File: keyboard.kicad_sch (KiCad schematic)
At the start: 14 parts, among them SW1 SW_SPDT, U1 STM32F072CBT6

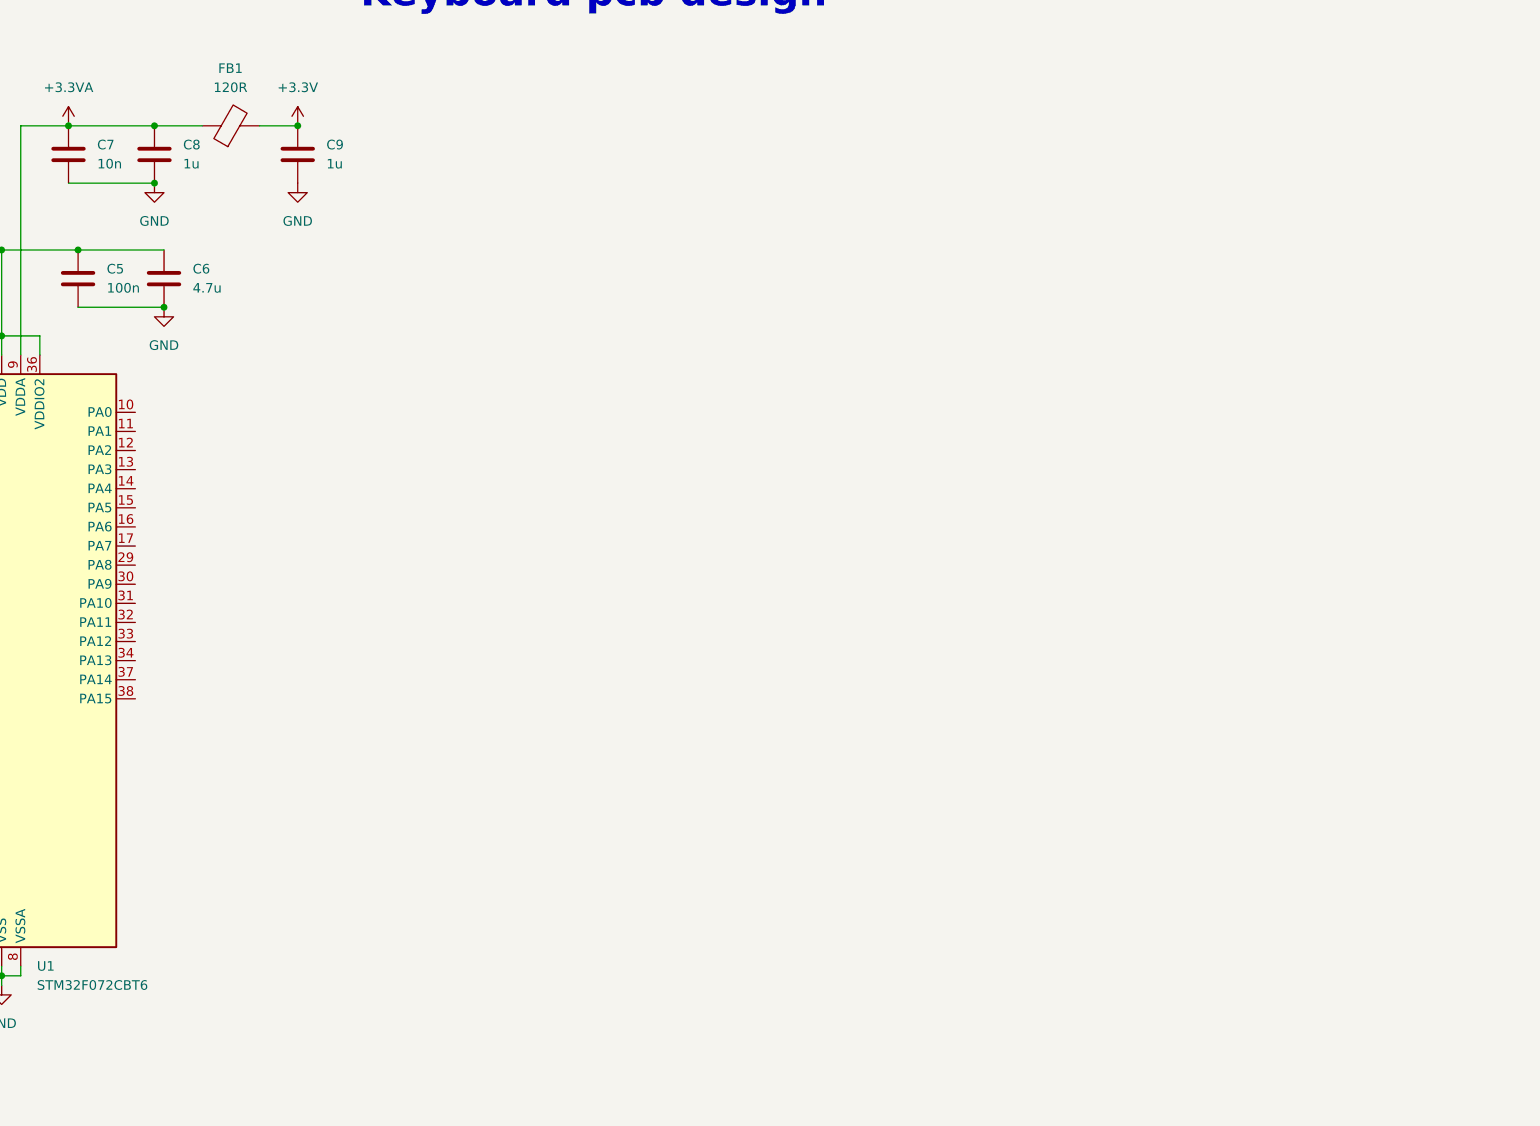
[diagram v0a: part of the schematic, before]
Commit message: Added keyboard matrix and leds
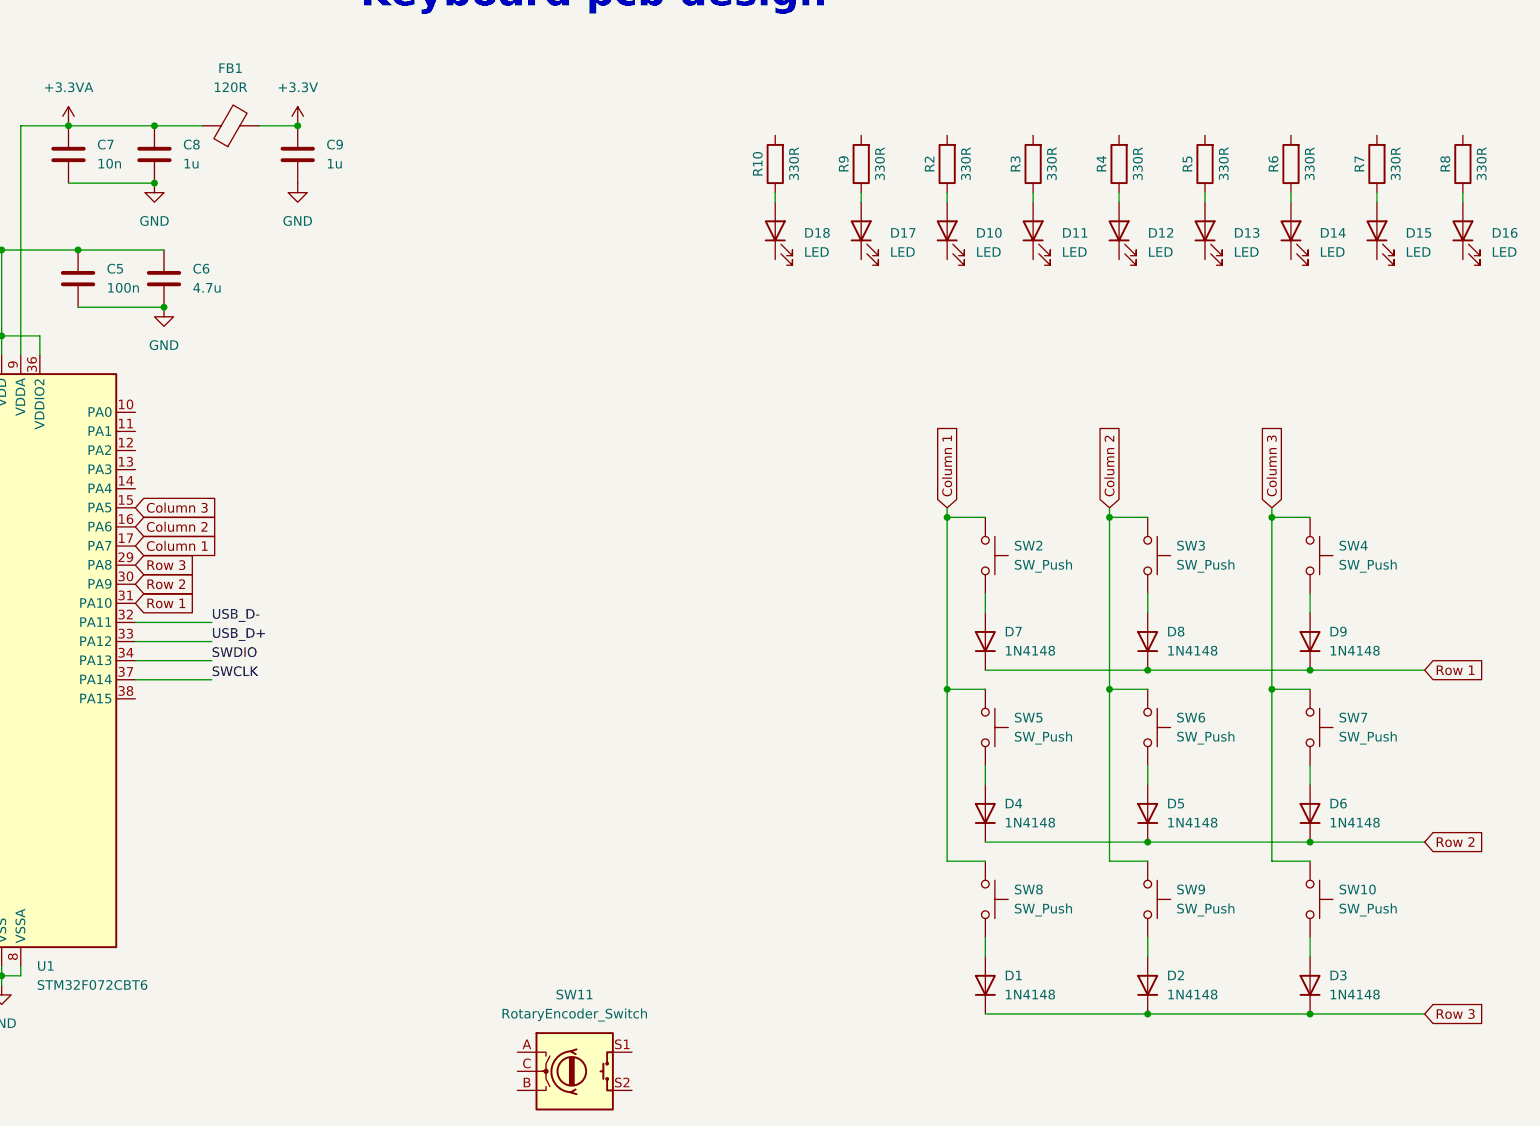
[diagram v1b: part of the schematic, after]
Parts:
- added D1, D2, D3, D4, D5, D6, D7, D8, D9: 1N4148, Diode_THT:D_DO-35_SOD27_P7.62mm_Horizontal, symbol Diode:1N4148
- added D10, D11, D12, D13, D14, D15, D16, D17, D18: LED, symbol Device:LED
- added R10, R2, R3, R4, R5, R6, R7, R8, R9: 330R, symbol Device:R
- added SW10, SW2, SW3, SW4, SW5, SW6, SW7, SW8, SW9: SW_Push, symbol Switch:SW_Push
- added SW11: RotaryEncoder_Switch, symbol Device:RotaryEncoder_Switch
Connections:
- net Column 3: now reaches U1.15 (PA5)
- net Column 3: now also SW10.1, SW4.1, SW7.1
- net Column 2: now reaches U1.16 (PA6)
- net Column 2: now also SW3.1, SW6.1, SW9.1
- net Column 1: now reaches U1.17 (PA7)
- net Column 1: now also SW2.1, SW5.1, SW8.1
- net Row 3: now reaches U1.29 (PA8)
- net Row 3: now also D1.1 (K), D2.1 (K), D3.1 (K)
- net Row 2: now reaches U1.30 (PA9)
- net Row 2: now also D4.1 (K), D5.1 (K), D6.1 (K)
- net Row 1: now reaches U1.31 (PA10)
- net Row 1: now also D7.1 (K), D8.1 (K), D9.1 (K)
- net USB_D-: now reaches U1.32 (PA11)
- net USB_D+: now reaches U1.33 (PA12)
- net SWDIO: now reaches U1.34 (PA13)
- net SWCLK: now reaches U1.37 (PA14)
- new net: D4.2 (A), SW5.2
- new net: D14.2 (A), R6.1
- new net: D18.2 (A), R10.1
- new net: D15.2 (A), R7.1
- new net: D17.2 (A), R9.1
- new net: D1.2 (A), SW8.2
- new net: D10.2 (A), R2.1
- new net: D13.2 (A), R5.1
- new net: D5.2 (A), SW6.2
- new net: D11.2 (A), R3.1
- new net: D6.2 (A), SW7.2
- new net: D2.2 (A), SW9.2
- new net: D16.2 (A), R8.1
- new net: D3.2 (A), SW10.2
- new net: D7.2 (A), SW2.2
- new net: D8.2 (A), SW3.2
- new net: D9.2 (A), SW4.2
- new net: D12.2 (A), R4.1

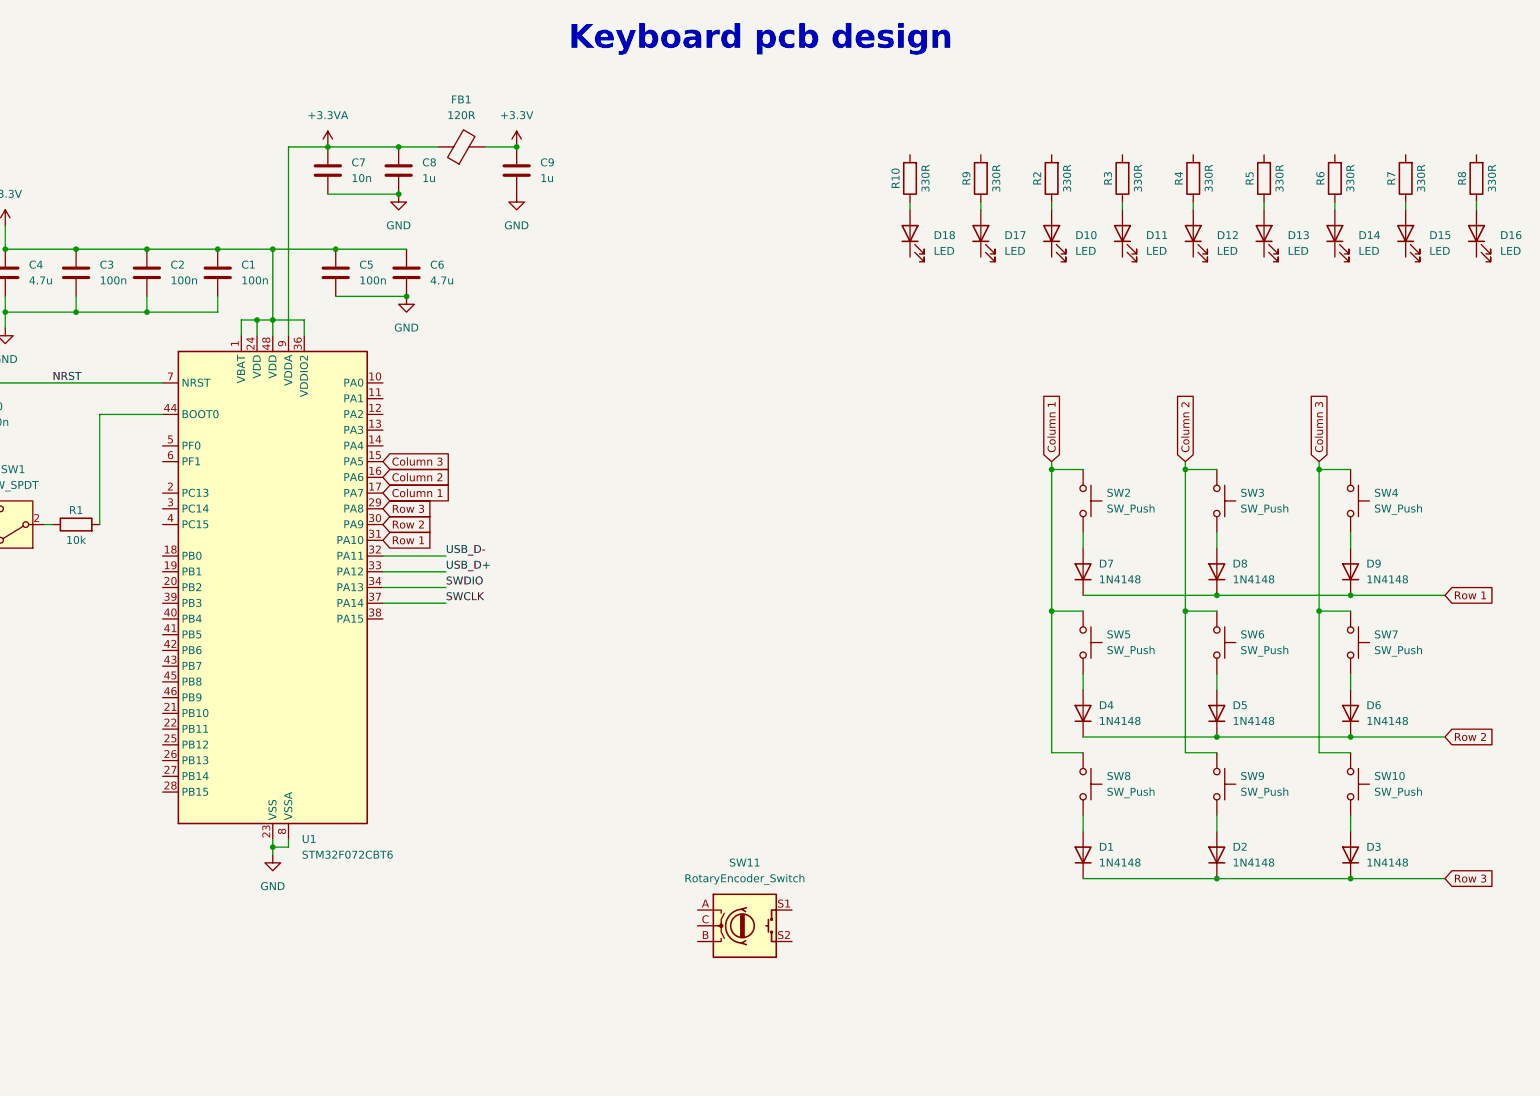
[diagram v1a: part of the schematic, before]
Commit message: Added rotary encoder
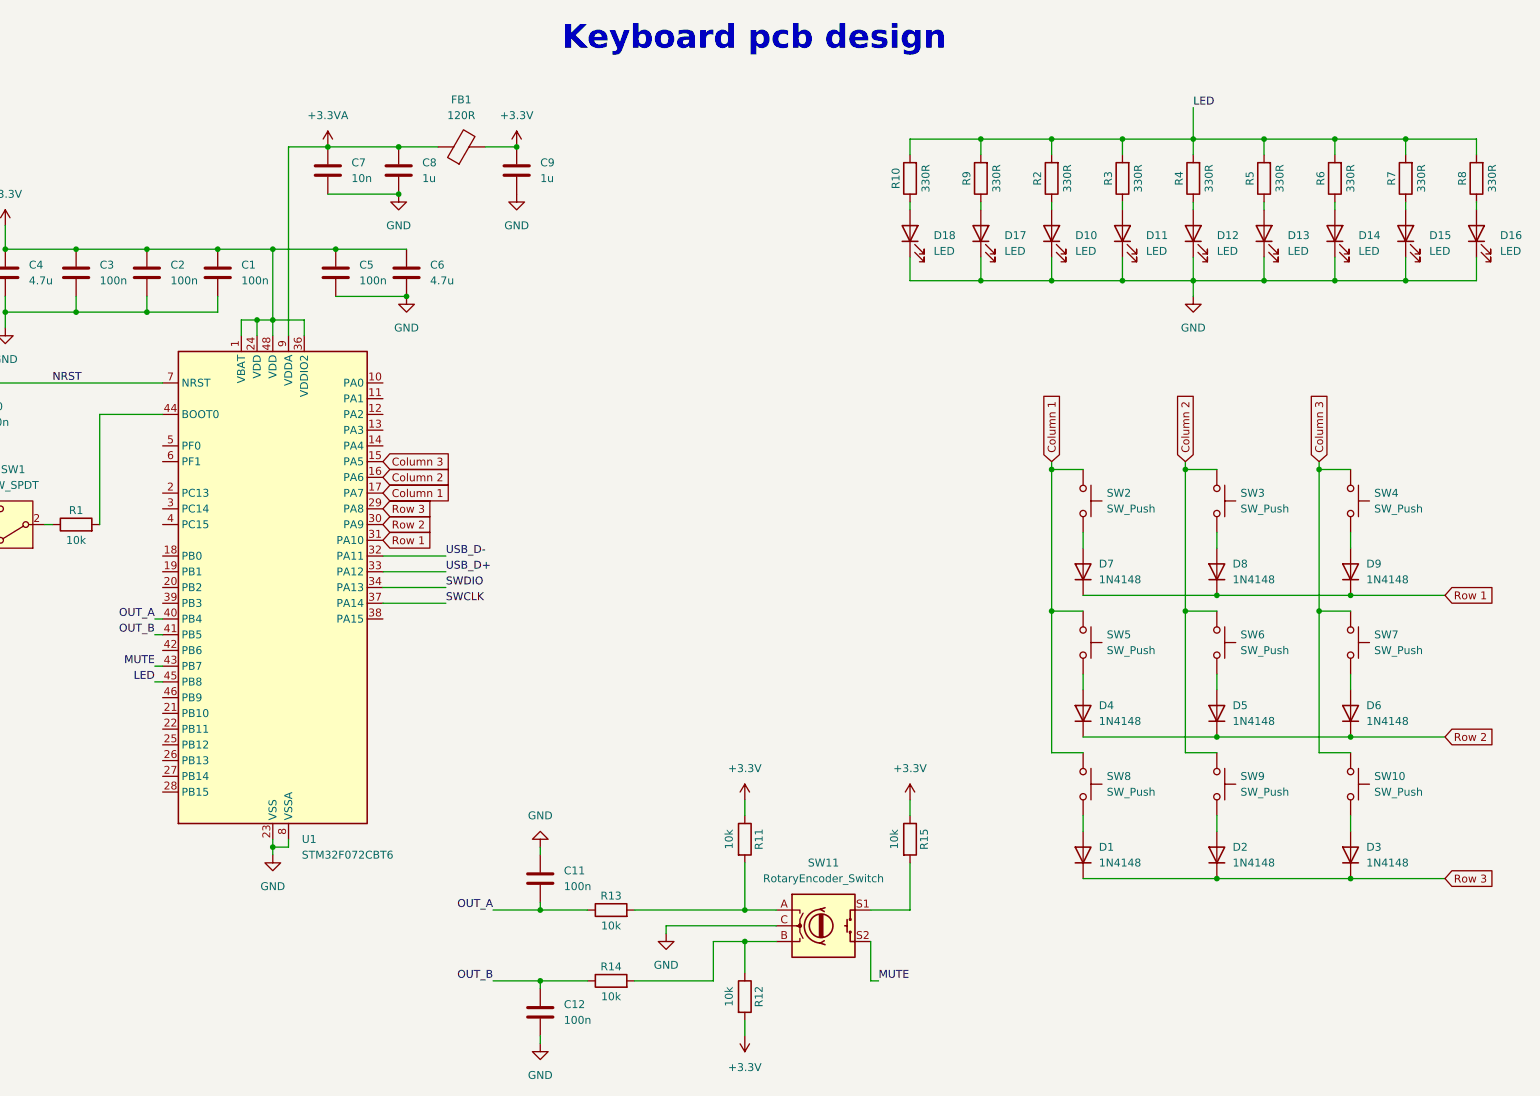
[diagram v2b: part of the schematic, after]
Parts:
- added C11, C12: 100n, symbol Device:C
- added R11, R12, R13, R14, R15: 10k, symbol Device:R
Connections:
- net +3.3V: now also R11.1, R12.2, R15.1
- net GND: now also D10.1 (K), D11.1 (K), D12.1 (K), D13.1 (K), D14.1 (K), D15.1 (K), D16.1 (K), D17.1 (K), D18.1 (K), SW11.C, C11.1, C12.2
- net LED: now reaches R10.2
- net LED: now also R2.2, R3.2, R4.2, R5.2, R6.2, R7.2, R8.2, R9.2, U1.45 (PB8)
- net at SW11.A: now also R11.2, R13.2
- net at SW11.B: now also R12.1, R14.2
- net at SW11.S1: now also R15.2
- net MUTE: now reaches SW11.S2
- net MUTE: now also U1.43 (PB7)
- net OUT_A: now reaches U1.40 (PB4)
- net OUT_A: now also C11.2, R13.1
- net OUT_B: now reaches U1.41 (PB5)
- net OUT_B: now also C12.1, R14.1
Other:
- moved on the sheet: SW11
